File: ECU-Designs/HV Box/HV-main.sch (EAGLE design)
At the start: 59 parts, among them IC2 MCP6002, IC3 MCP6002, T1 120, T2 120, X1 MINIFIT_5566-8

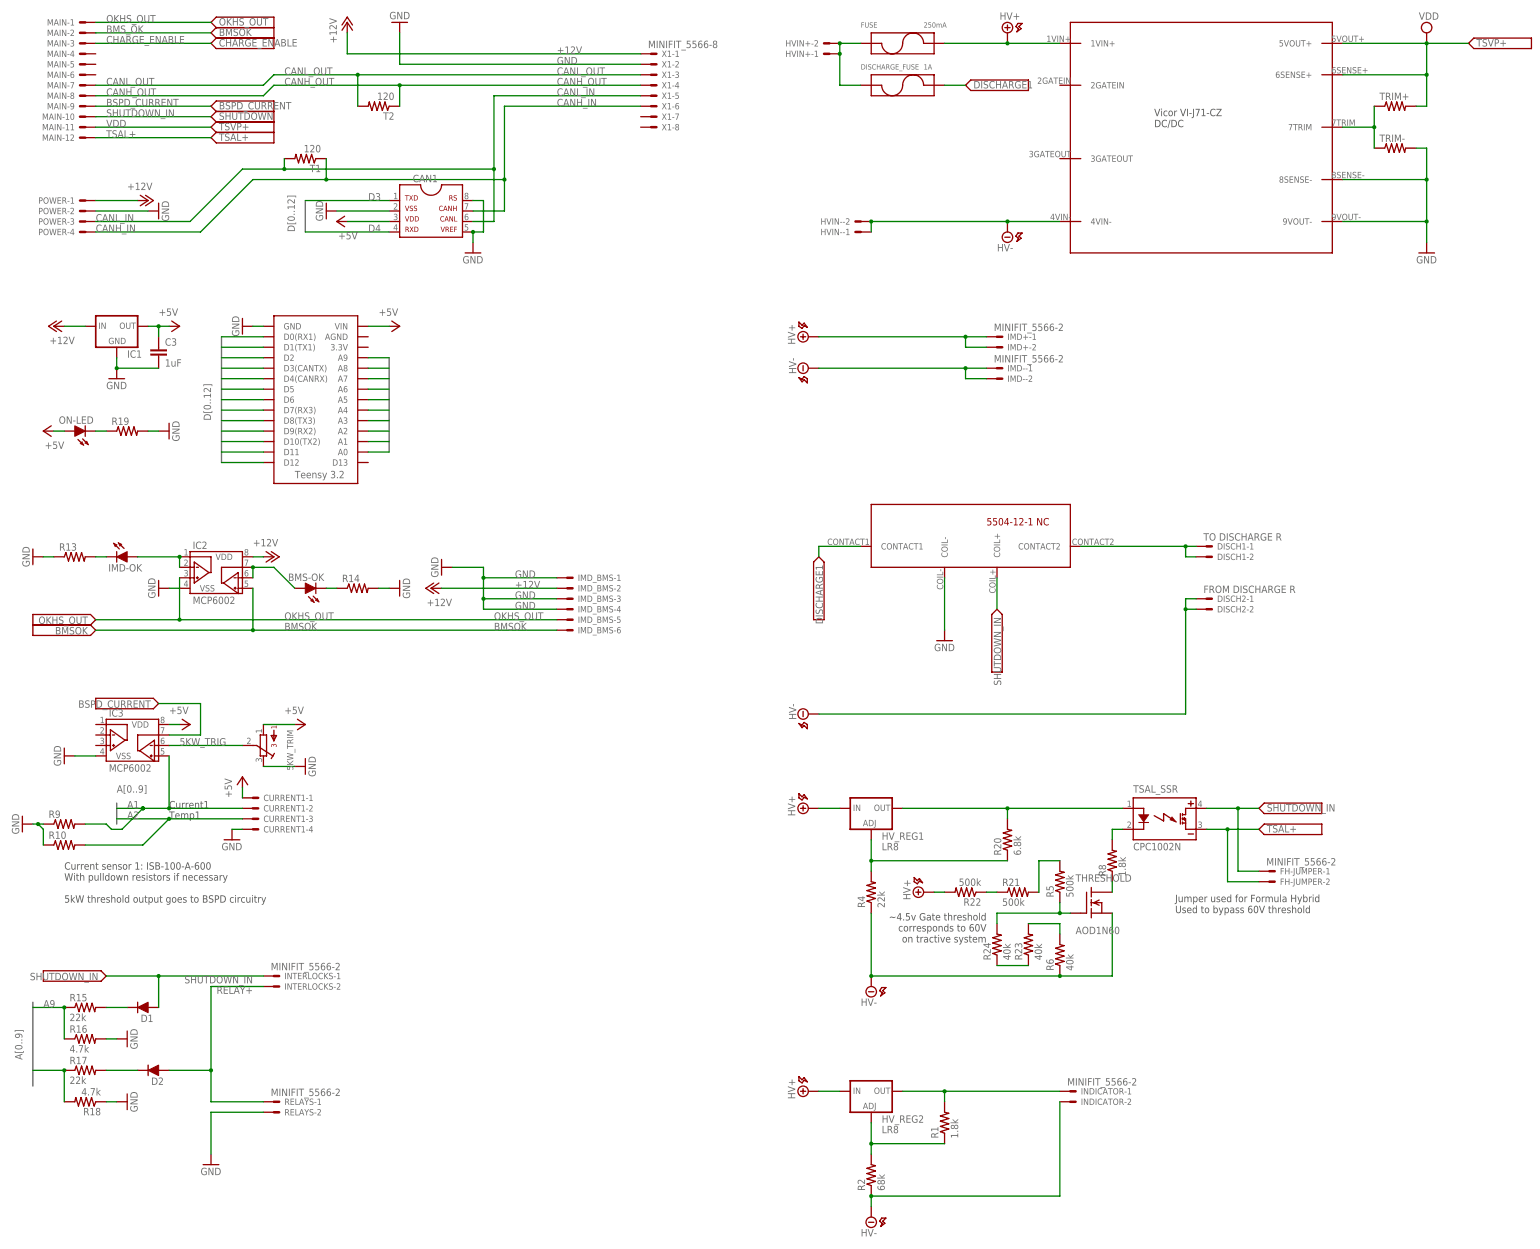
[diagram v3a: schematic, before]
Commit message: Power board: add gnd, remove unneeded diode; External diagram: update HV PCB wiring and power board wiring; HV board: changes to meet rules, clearer HV naming, remove microcontroller
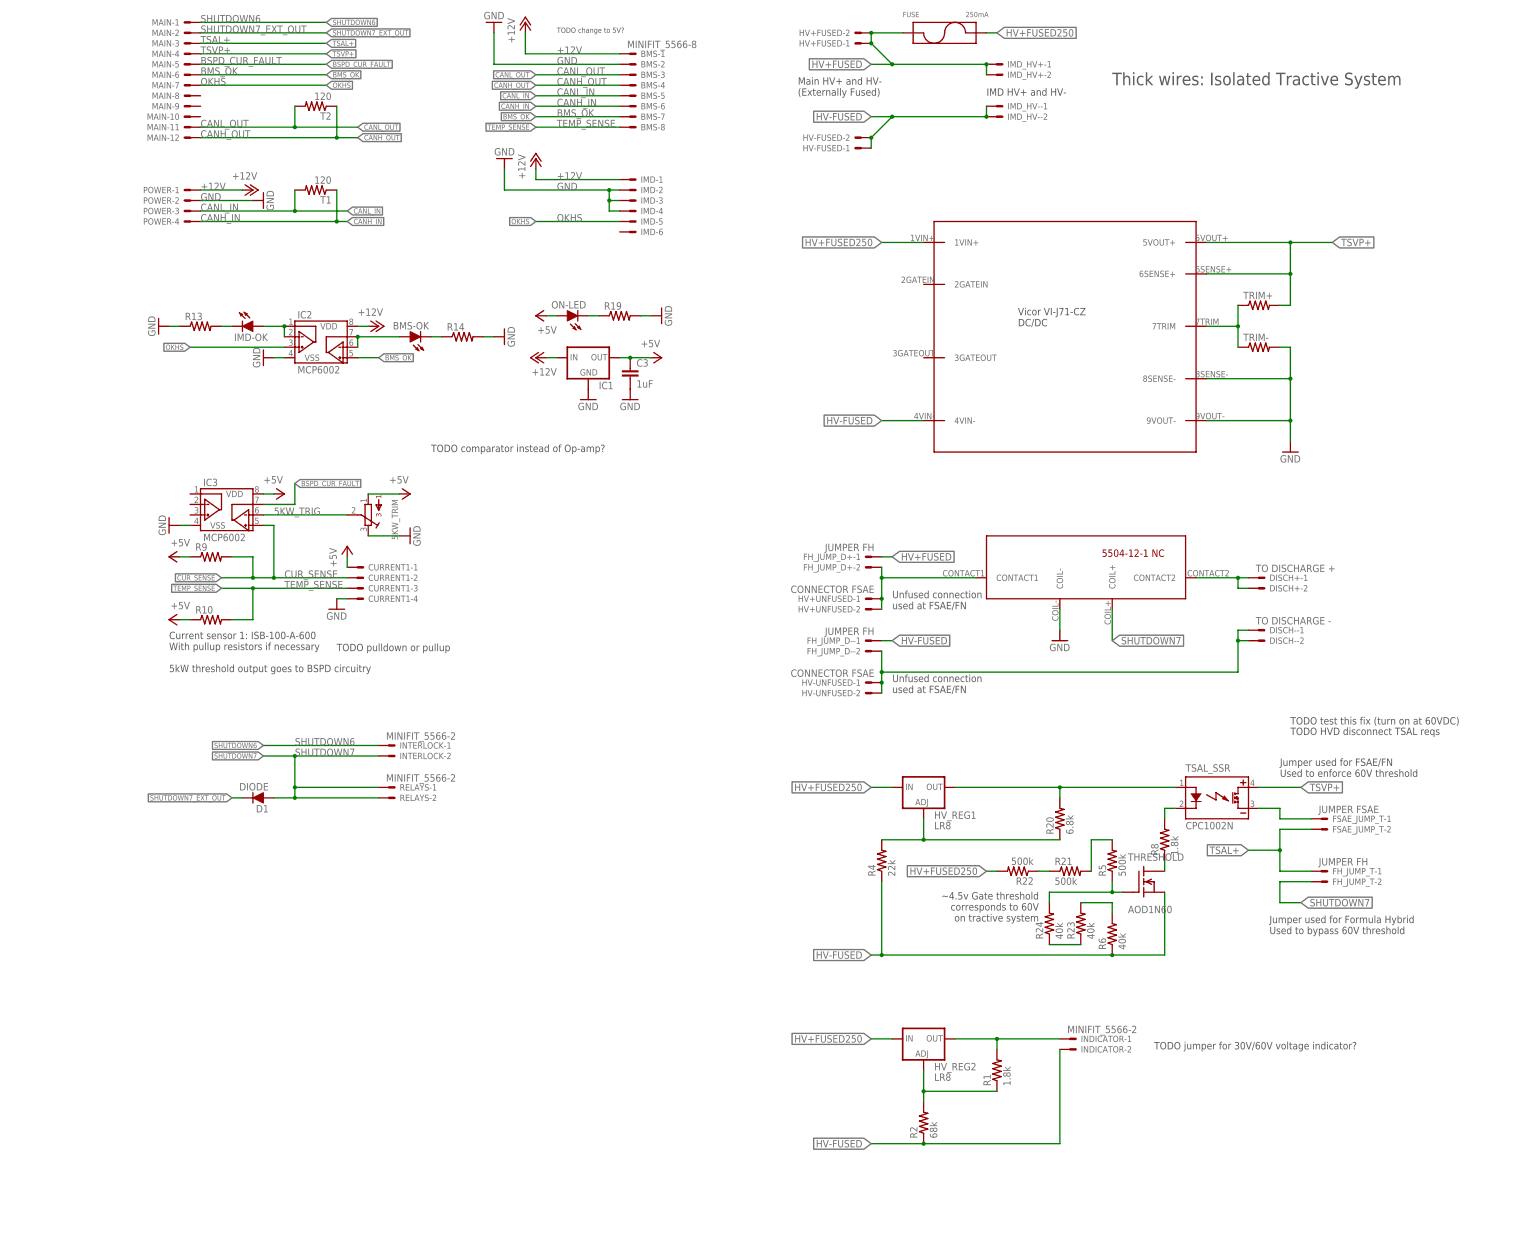
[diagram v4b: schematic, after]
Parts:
- removed CAN1: MCP2551, HyTechDevices:MCP2551
- removed D2: DIODE0805, HyTechDevices:DIODE0805
- removed DISCH1: TO DISCHARGE R, HyTechDevices:MINIFIT_5566-2
- removed DISCH2: FROM DISCHARGE R, HyTechDevices:MINIFIT_5566-2
- removed DISCHARGE_FUSE: 1A, HyTechDevices:FUSE_5X20MM
- removed FH-JUMPER, HVIN+, HVIN-, IMD+, IMD-, INTERLOCKS: MINIFIT_5566-2, HyTechDevices:MINIFIT_5566-2
- removed IMD_BMS: MINIFIT_5566-6, HyTechDevices:MINIFIT_5566-6
- removed R15, R17: 22k, HyTechDevices:RESISTOR0805-RES
- removed R16, R18: 4.7k, HyTechDevices:RESISTOR0805-RES
- removed U$2: TEENSY_3.2_SIMPLE, HyTechDevices:TEENSY_3.2_SIMPLE
- removed X1: MINIFIT_5566-8, HyTechDevices:MINIFIT_5566-8
- added BMS: MINIFIT_5566-8, HyTechDevices:MINIFIT_5566-8
- added DISCH+: TO DISCHARGE +, HyTechDevices:MINIFIT_5566-2
- added DISCH-: TO DISCHARGE -, HyTechDevices:MINIFIT_5566-2
- added FH_JUMP_D+, FH_JUMP_D-: JUMPER FH, HyTechDevices:CONNECTOR-2
- added FH_JUMP_T: JUMPER FH, HyTechDevices:MINIFIT_5566-2
- added FSAE_JUMP_T: JUMPER FSAE, HyTechDevices:MINIFIT_5566-2
- added HV+FUSED, HV-FUSED, INTERLOCK: MINIFIT_5566-2, HyTechDevices:MINIFIT_5566-2
- added HV+UNFUSED, HV-UNFUSED: CONNECTOR FSAE, HyTechDevices:CONNECTOR-2
- added IMD: CONNECTOR-6, HyTechDevices:CONNECTOR-6
- added IMD_HV+, IMD_HV-: CONNECTOR-2, HyTechDevices:CONNECTOR-2
- D1: value DIODE0805 -> DIODE; device HyTechDevices:DIODE0805 -> HyTechDevices:DIODEDO-41
- MAIN: value MINIFIT_5566-12 -> CONNECTOR-12; device HyTechDevices:MINIFIT_5566-12 -> HyTechDevices:CONNECTOR-12
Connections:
- removed net A0: U$2.A0
- removed net A1: CURRENT1-2.S, IC3.VINB+, R9.2, U$2.A1
- removed net A2: CURRENT1-3.S, R10.2, U$2.A2
- removed net A3: U$2.A3
- removed net A4: U$2.A4
- removed net A5: U$2.A5
- removed net A6: U$2.A6
- removed net A7: U$2.A7
- removed net A8: R17.1, R18.2, U$2.A8
- removed net A9: R15.1, R16.1, U$2.A9
- removed net BMSOK: IC2.VINB+, IMD_BMS-6.S
- removed net BSPD_CURRENT: IC3.VOUTB, MAIN-9.S
- removed net CHARGE_ENABLE: MAIN-3.S
- removed net D0: U$2.D0(RX1)
- removed net D1: U$2.D1(TX1)
- removed net D10: U$2.D10(TX2)
- removed net D11: U$2.D11
- removed net D12: U$2.D12
- removed net D2: U$2.D2
- removed net D3: CAN1.1, U$2.D3(CANTX)
- removed net D4: CAN1.4, U$2.D4(CANRX)
- removed net D5: U$2.D5
- removed net D6: U$2.D6
- removed net D7: U$2.D7(RX3)
- removed net D8: U$2.D8(TX3)
- removed net D9: U$2.D9(RX2)
- removed net HV+: FUSE.P2, HV_REG1.IN, HV_REG2.IN, IMD+-1.S, IMD+-2.S, R22.2, U$5.1VIN+
- removed net HV-: DISCH2-1.S, DISCH2-2.S, HVIN--1.S, HVIN--2.S, IMD--1.S, IMD--2.S, INDICATOR-2.S, R2.1, R4.1, R6.1, THRESHOLD.S, U$5.4VIN-
- removed net HVIN+: DISCHARGE_FUSE.P1, FUSE.P1, HVIN+-1.S, HVIN+-2.S
- removed net N$5: D2.C, R17.2
- removed net OKHS_OUT: IC2.VINA+, IMD_BMS-5.S, MAIN-1.S
- removed net RELAY+: D2.A, INTERLOCKS-2.S, RELAYS-1.S
- removed net SHUTDOWN_IN: D1.A, FH-JUMPER-1.S, INTERLOCKS-1.S, MAIN-10.S, TSAL_SSR.DC+, U$12.COIL+
- removed net VDD: MAIN-11.S, TRIM+.2, U$5.5VOUT+, U$5.6SENSE+
- new net BSPD_CUR_FAULT: IC3.VOUTB, MAIN-5.S
- new net CUR_SENSE: CURRENT1-2.S, IC3.VINB+, R9.2
- new net DISCHARGE3: DISCH--1.S, DISCH--2.S, FH_JUMP_D--2.S, HV-UNFUSED-1.S, HV-UNFUSED-2.S
- new net HV+FUSED: FH_JUMP_D+-1.S, FUSE.P1, HV+FUSED-1.S, HV+FUSED-2.S, IMD_HV+-1.S, IMD_HV+-2.S
- new net HV+FUSED250: FUSE.P2, HV_REG1.IN, HV_REG2.IN, R22.2, U$5.1VIN+
- new net HV-FUSED: FH_JUMP_D--1.S, HV-FUSED-1.S, HV-FUSED-2.S, IMD_HV--1.S, IMD_HV--2.S, INDICATOR-2.S, R2.1, R4.1, R6.1, THRESHOLD.S, U$5.4VIN-
- new net OKHS: IC2.VINA+, IMD-5.S, MAIN-7.S
- new net SHUTDOWN6: INTERLOCK-1.S, MAIN-1.S
- new net SHUTDOWN7: D1.A, FH_JUMP_T-2.S, INTERLOCK-2.S, RELAYS-1.S, RELAYS-2.S, U$12.COIL+
- new net SHUTDOWN7_EXT_OUT: D1.C, MAIN-2.S
- new net TEMP_SENSE: BMS-8.S, CURRENT1-3.S, R10.2
- new net TSVP+: MAIN-4.S, TRIM+.2, TSAL_SSR.DC+, U$5.5VOUT+, U$5.6SENSE+
- net +12V: now also BMS-1.S, IMD-1.S; no longer IMD_BMS-2.S, X1-1.S
- net +5V: now also R10.1, R9.1; no longer CAN1.3, U$2.VIN
- net BMS_OK: now also BMS-7.S, IC2.VINB+, MAIN-6.S; no longer MAIN-2.S
- net CANH_IN: now also BMS-6.S; no longer CAN1.7, X1-6.S
- net CANH_OUT: now also BMS-4.S, MAIN-12.S; no longer MAIN-8.S, X1-4.S
- net CANL_IN: now also BMS-5.S; no longer CAN1.6, X1-5.S
- net CANL_OUT: now also BMS-3.S, MAIN-11.S; no longer MAIN-7.S, X1-3.S
- net DISCHARGE1: now also FH_JUMP_D+-2.S, HV+UNFUSED-1.S, HV+UNFUSED-2.S; no longer DISCHARGE_FUSE.P2
- net DISCHARGE2: now also DISCH+-1.S, DISCH+-2.S; no longer DISCH1-1.S, DISCH1-2.S
- net GND: now also BMS-2.S, IMD-2.S, IMD-3.S, IMD-4.S; no longer CAN1.2, CAN1.5, CAN1.8, IMD_BMS-1.S, IMD_BMS-3.S, IMD_BMS-4.S, R10.1, R16.2, R18.1, R9.1, RELAYS-2.S, U$2.GND, X1-2.S
- net N$4: now also FSAE_JUMP_T-1.S, TSAL_SSR.DC-; no longer D1.C, R15.2
- net TSAL+: now also FH_JUMP_T-1.S, FSAE_JUMP_T-2.S, MAIN-3.S; no longer FH-JUMPER-2.S, MAIN-12.S, TSAL_SSR.DC-
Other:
- note added: "Current sensor 1: ISB-100-A-600 With pullup resistors if necessary 5kW threshold output goes to BSPD circuitry"
- note added: "IMD HV+ and HV-"
- note added: "Jumper used for FSAE/FN Used to enforce 60V threshold"
- note added: "LEDs"
- note added: "Main HV+ and HV- (Externally Fused)"
- note added: "TODO HVD disconnect TSAL reqs"
- note added: "TODO change to 5V?"
- note added: "TODO comparator instead of Op-amp?"
- note added: "TODO jumper for 30V/60V voltage indicator?"
- note added: "TODO pulldown or pullup"
- note added: "TODO test this fix (turn on at 60VDC)"
- note added: "TS I/O"
- note added: "Thick wires: Isolated Tractive System"
- note added: "Unfused connection used at FSAE/FN"
- note removed: "BMS & IMD Routing"
- note removed: "Current sensor 1: ISB-100-A-600 With pulldown resistors if necessary 5kW threshold output goes to BSPD circuitry"
- note removed: "Current1"
- note removed: "IMD Connections"
- note removed: "Microcontroller"
- note removed: "Temp1"
- moved on the sheet: 5KW_TRIM, BMS-OK, C3, CURRENT1-1, CURRENT1-2, CURRENT1-3, CURRENT1-4, D1, FUSE, HV_REG1, HV_REG2, IC1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

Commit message: Update accumulator indicator / tsal control circuitry
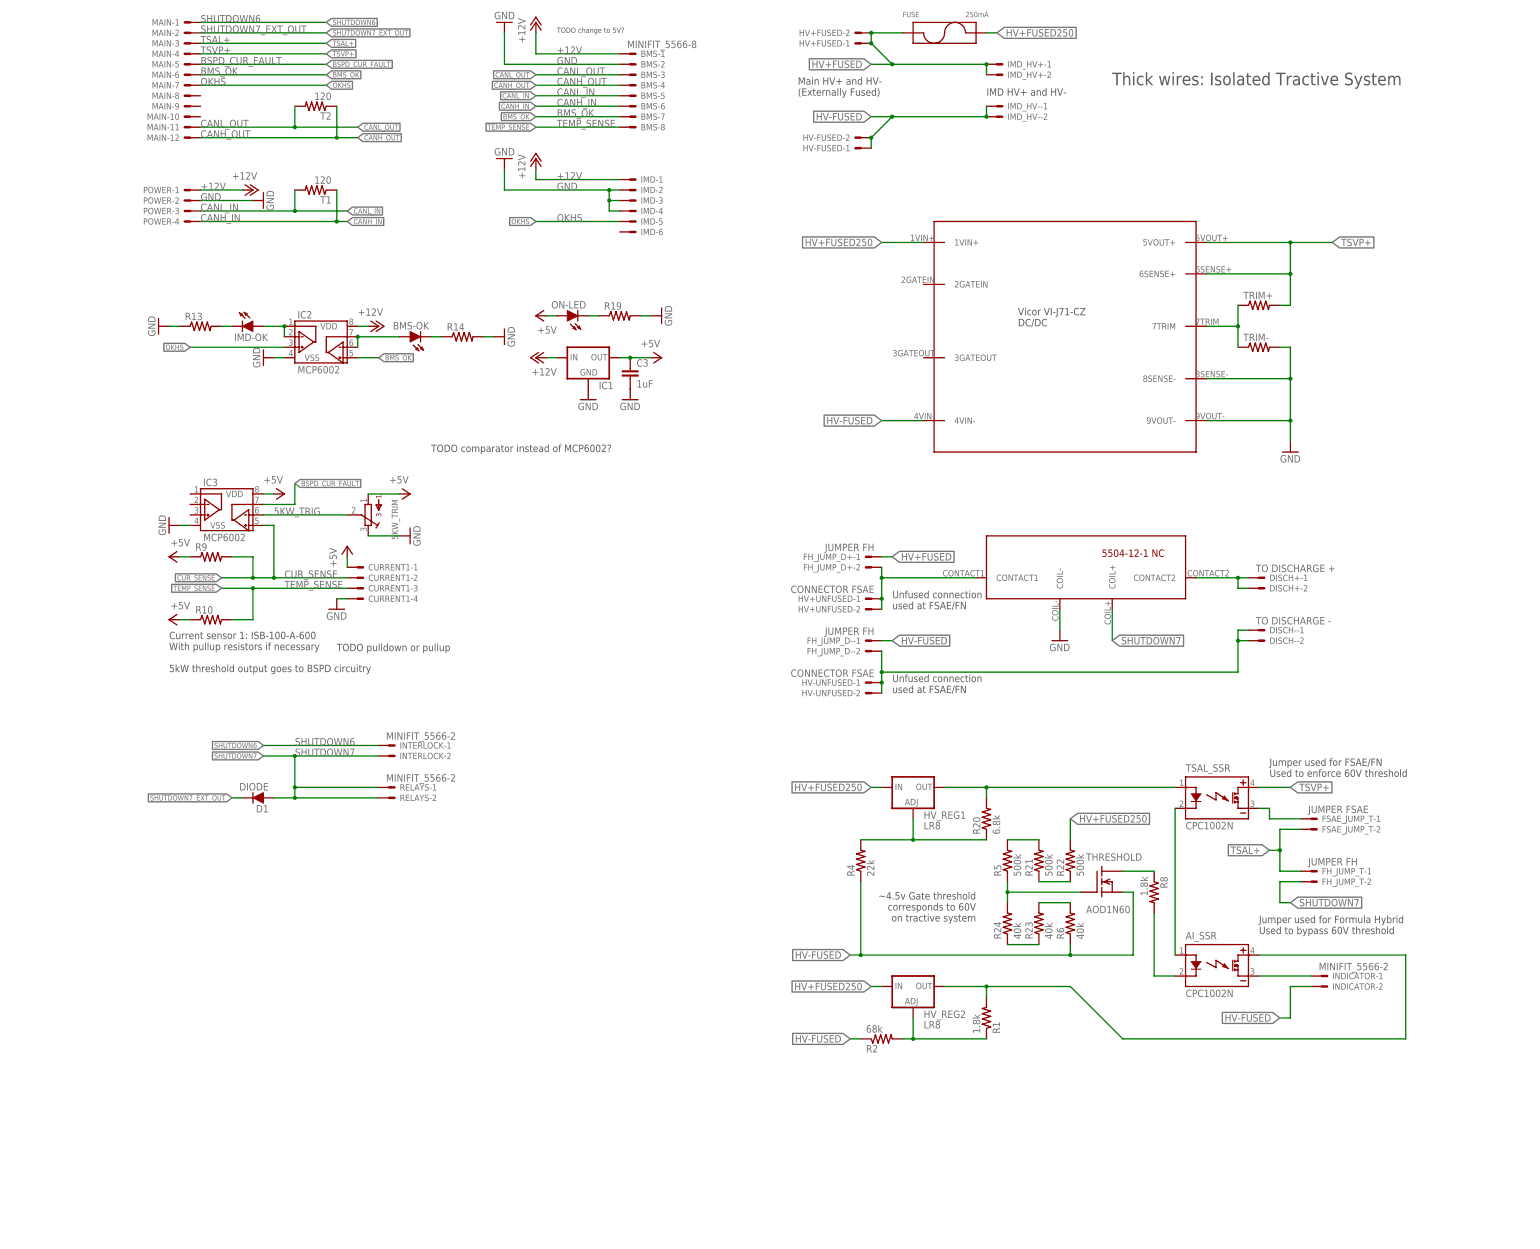
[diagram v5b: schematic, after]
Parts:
- added AI_SSR: CPC1002N, HyTechDevices:CPC1002N
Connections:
- removed net N$41: R8.2, TSAL_SSR.CONTROL-
- new net N$5: AI_SSR.CONTROL-, R8.2
- new net N$6: AI_SSR.CONTROL+, TSAL_SSR.CONTROL-
- new net N$7: AI_SSR.DC-, INDICATOR-1.S
- net N$1: now also AI_SSR.DC+; no longer INDICATOR-1.S
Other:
- note added: "TODO comparator instead of MCP6002?"
- note added: "TSAL/TSEL Control, Accumulator Voltage Indicator"
- note removed: "Accumulator Voltage Present Indicator"
- note removed: "TODO HVD disconnect TSAL reqs"
- note removed: "TODO comparator instead of Op-amp?"
- note removed: "TODO jumper for 30V/60V voltage indicator?"
- note removed: "TODO test this fix (turn on at 60VDC)"
- note removed: "TSAL/TSEL Control"
- moved on the sheet: FH_JUMP_T-1, FH_JUMP_T-2, FSAE_JUMP_T-1, FSAE_JUMP_T-2, HV_REG1, HV_REG2, INDICATOR-1, INDICATOR-2, R1, R2, R20, R21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
